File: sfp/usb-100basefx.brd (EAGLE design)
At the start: 54 x 29 mm, 52 parts, among them IC1 LD33, IC2 93LC66SN, U1 AX88772BSP, U2 SFP, Y1 25MHz

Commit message: there's a cat on my pcb...
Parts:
- added U$2, U$4, U$8: (no value), cat:CAT-L
- added U$3, U$5, U$7: (no value), cat:CAT-R
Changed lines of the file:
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@@
 <element name="R1" library="rcl" package="R0603" value="0" x="15.6464" y="8.9408" rot="MR0"/>
 <element name="R3" library="rcl" package="R0603" value="0" x="15.6464" y="7.5184" rot="MR0"/>
+<element name="U$2" library="cat" package="CAT-L" value="" x="12.192" y="27.0256" rot="R270"/>
+<element name="U$3" library="cat" package="CAT-R" value="" x="19.1008" y="23.9776" rot="R270"/>
+<element name="U$4" library="cat" package="CAT-L" value="" x="23.5712" y="27.0256" rot="R270"/>
+<element name="U$5" library="cat" package="CAT-R" value="" x="27.6352" y="24.9936" rot="R270"/>
+<element name="U$7" library="cat" package="CAT-R" value="" x="42.2656" y="24.5872" rot="R270"/>
+<element name="U$8" library="cat" package="CAT-L" value="" x="45.5168" y="27.0256" rot="R270"/>
 </elements>
 <signals>

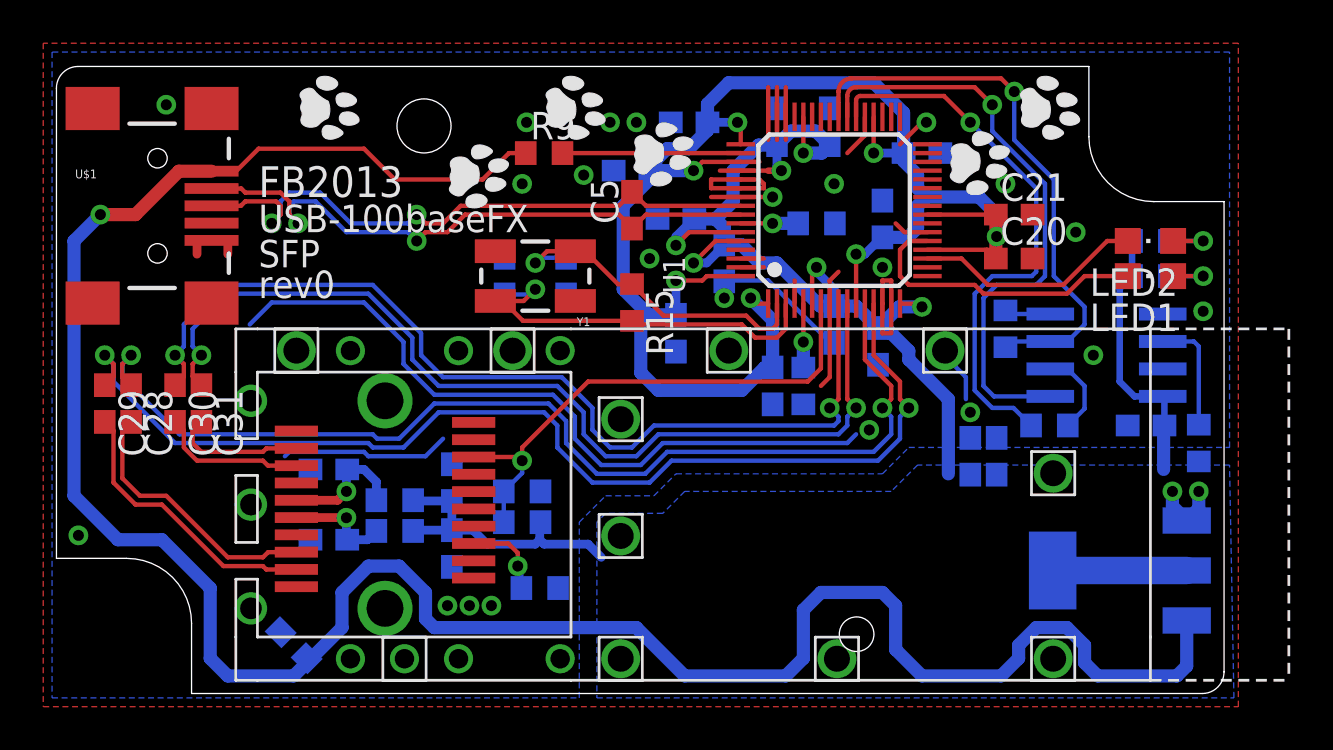
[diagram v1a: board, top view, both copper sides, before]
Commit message: rev1: fix sd signal logic level
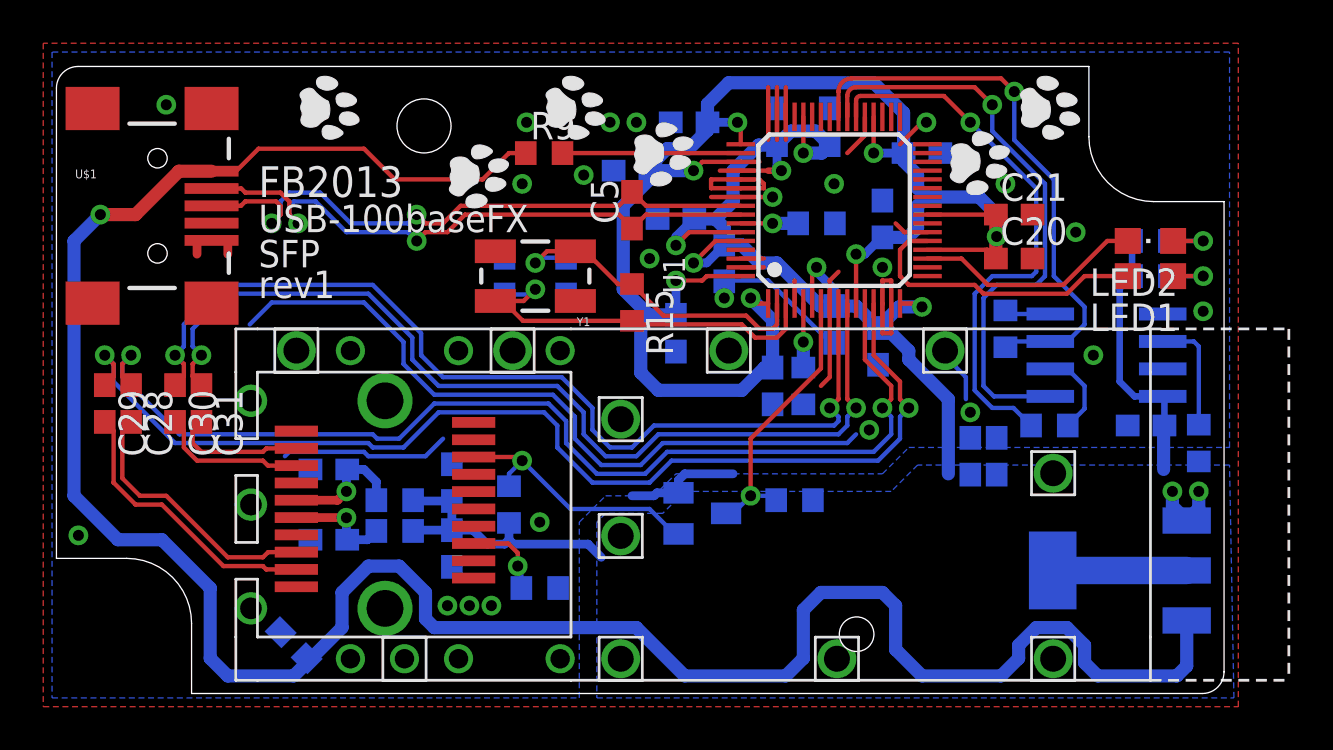
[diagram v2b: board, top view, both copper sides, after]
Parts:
- added Q1: MOSFET-NCHANNELBSS123LT1G, SparkFun-DiscreteSemi:SOT23
- moved R21 12.6 mm to (34.1, 8.94), turned to 0 degrees
- moved R20 1.02 mm to (20.9, 8.74), turned to 90 degrees
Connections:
- new net SD_OUT: Q1.3, R21.2, U1.7
- net GND: now also Q1.2; no longer R21.2
- net SD: now also Q1.1; no longer R21.1, U1.7
- net VCC: now also R21.1
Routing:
- net SD_OUT: track 0.00 -> 13.0 mm, vias 0 -> 1
- net SD: track 24.4 -> 12.4 mm
- net GND: track 90.2 -> 95.7 mm, vias 24 -> 25
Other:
- board text added: "rev1"
- board text removed: "rev0"
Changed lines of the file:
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@@
 <text x="9.3472" y="21.336" size="1.27" layer="121">USB-100baseFX</text>
 <text x="9.3472" y="19.7104" size="1.27" layer="121">SFP</text>
-<text x="9.3472" y="18.288" size="1.27" layer="121">rev0</text>
+<text x="9.3472" y="18.288" size="1.27" layer="121">rev1</text>
 <hole x="37.0078" y="2.7432" drill="1.6"/>
 </plain>
@@
 <element name="C26" library="rcl" package="C0603" value=".1u" x="40.0304" y="24.9936" rot="MR180"/>
 <element name="C27" library="rcl" package="C0603" value=".1u" x="42.2656" y="10.9728" rot="MR90"/>
-<element name="R20" library="rcl" package="R0603" value="130" x="21.5392" y="7.9248" rot="MR0"/>
-<element name="R21" library="rcl" package="R0603" value="82" x="21.5392" y="9.3472" rot="MR180"/>
+<element name="R20" library="rcl" package="R0603" value="130" x="20.9296" y="8.7376" rot="MR90"/>
+<element name="R21" library="rcl" package="R0603" value="82" x="34.1376" y="8.9408" rot="MR0"/>
 <element name="IC1" library="SparkFun-PowerIC" package="SOT223" value="LD33" x="49.1744" y="5.6896" rot="MR270"/>
 <element name="C9" library="rcl" package="C0603" value=".1u" x="18.288" y="6.7056" rot="MR270"/>
@@
 <element name="U$7" library="cat" package="CAT-R" value="" x="42.2656" y="24.5872" rot="R270"/>
 <element name="U$8" library="cat" package="CAT-L" value="" x="45.5168" y="27.0256" rot="R270"/>
+<element name="Q1" library="SparkFun-DiscreteSemi" package="SOT23" value="MOSFET-NCHANNELBSS123LT1G" x="29.8704" y="8.3312" rot="MR90">
+<attribute name="PROD_ID" value="TRANS-08345" x="29.8704" y="8.3312" size="1.778" layer="28" rot="MR90" display="off"/>
+</element>
 </elements>
 <signals>
@@
 <wire x1="18.288" y1="7.5556" x2="19.2668" y2="7.5556" width="0.4064" layer="16"/>
 <wire x1="19.2668" y1="7.5556" x2="19.9136" y2="6.9088" width="0.4064" layer="16"/>
-<wire x1="19.9136" y1="6.9088" x2="22.1488" y2="6.9088" width="0.4064" layer="16"/>
-<wire x1="22.1488" y1="6.9088" x2="22.352" y2="7.112" width="0.4064" layer="16"/>
-<wire x1="22.352" y1="7.112" x2="22.5552" y2="6.9088" width="0.4064" layer="16"/>
-<wire x1="22.5552" y1="6.9088" x2="24.5872" y2="6.9088" width="0.4064" layer="16"/>
+<wire x1="19.9136" y1="6.9088" x2="20.7264" y2="6.9088" width="0.4064" layer="16"/>
+<wire x1="20.7264" y1="6.9088" x2="20.9296" y2="7.112" width="0.4064" layer="16"/>
+<wire x1="20.9296" y1="7.112" x2="21.1328" y2="6.9088" width="0.4064" layer="16"/>
+<wire x1="21.1328" y1="6.9088" x2="24.5872" y2="6.9088" width="0.4064" layer="16"/>
 <wire x1="24.5872" y1="6.9088" x2="25.1968" y2="6.2992" width="0.4064" layer="16"/>
-<wire x1="22.352" y1="7.112" x2="22.352" y2="7.8876" width="0.4064" layer="16"/>
-<wire x1="22.352" y1="7.8876" x2="22.3892" y2="7.9248" width="0.4064" layer="16"/>
 <wire x1="39.4208" y1="15.8496" x2="39.4208" y2="15.4432" width="0.6096" layer="16"/>
 <wire x1="39.4208" y1="15.4432" x2="41.2496" y2="13.6144" width="0.6096" layer="16"/>
@@
 <wire x1="18.288" y1="8.9036" x2="16.5336" y2="8.9036" width="0.4064" layer="16"/>
 <wire x1="16.5336" y1="8.9036" x2="16.4964" y2="8.9408" width="0.4064" layer="16"/>
+<contactref element="R21" pad="1"/>
+<wire x1="20.9296" y1="7.112" x2="20.9296" y2="7.8876" width="0.4064" layer="16"/>
 </signal>
 <signal name="GND">
@@
 <contactref element="C27" pad="2"/>
 <via x="5.08" y="27.2288" extent="1-16" drill="0.508"/>
-<contactref element="R21" pad="2"/>
 <contactref element="IC1" pad="1"/>
 <wire x1="7.9248" y1="20.9552" x2="7.9248" y2="20.32" width="0.4064" layer="1"/>
@@
 <wire x1="35.7632" y1="18.034" x2="35.7632" y2="14.6304" width="0.2032" layer="1"/>
 <wire x1="35.7632" y1="14.6304" x2="35.3568" y2="14.224" width="0.2032" layer="1"/>
+<contactref element="Q1" pad="2"/>
+<via x="22.352" y="7.9248" extent="1-16" drill="0.508"/>
+<wire x1="28.7704" y1="9.2812" x2="27.7724" y2="9.2812" width="0.4064" layer="16"/>
+<wire x1="28.7704" y1="9.2812" x2="28.7704" y2="9.8728" width="0.4064" layer="16"/>
+<wire x1="28.7704" y1="9.8728" x2="29.0576" y2="10.16" width="0.4064" layer="16"/>
+<wire x1="29.0576" y1="10.16" x2="31.2928" y2="10.16" width="0.4064" layer="16"/>
+<wire x1="27.7724" y1="9.2812" x2="27.6352" y2="9.144" width="0.4064" layer="16"/>
+<wire x1="27.6352" y1="9.144" x2="26.6192" y2="9.144" width="0.4064" layer="16"/>
 </signal>
 <signal name="TD_DP">
@@
 </signal>
 <signal name="SD">
-<contactref element="U1" pad="7"/>
-<contactref element="R21" pad="1"/>
 <contactref element="R20" pad="2"/>
-<wire x1="20.6892" y1="9.3472" x2="20.6892" y2="7.9248" width="0.2032" layer="16"/>
-<wire x1="35.3568" y1="18.034" x2="35.3568" y2="15.0368" width="0.2032" layer="1"/>
 <contactref element="U2" pad="8"/>
 <via x="21.5392" y="10.7696" extent="1-16" drill="0.508"/>
-<wire x1="35.3568" y1="15.0368" x2="34.7472" y2="14.4272" width="0.2032" layer="1"/>
-<wire x1="34.7472" y1="14.4272" x2="24.5872" y2="14.4272" width="0.2032" layer="1"/>
-<wire x1="24.5872" y1="14.4272" x2="21.5392" y2="11.3792" width="0.2032" layer="1"/>
-<wire x1="21.5392" y1="11.3792" x2="21.5392" y2="10.7696" width="0.2032" layer="1"/>
-<wire x1="20.6892" y1="9.3472" x2="21.5392" y2="10.1972" width="0.2032" layer="16"/>
-<wire x1="21.5392" y1="10.1972" x2="21.5392" y2="10.7696" width="0.2032" layer="16"/>
 <wire x1="19.2968" y1="10.9376" x2="21.3712" y2="10.9376" width="0.2032" layer="1"/>
 <wire x1="21.3712" y1="10.9376" x2="21.5392" y2="10.7696" width="0.2032" layer="1"/>
+<contactref element="Q1" pad="1"/>
+<wire x1="20.9296" y1="9.5876" x2="20.9296" y2="10.16" width="0.2032" layer="16"/>
+<wire x1="20.9296" y1="10.16" x2="21.5392" y2="10.7696" width="0.2032" layer="16"/>
+<wire x1="21.5392" y1="10.7696" x2="23.7744" y2="8.5344" width="0.2032" layer="16"/>
+<wire x1="23.7744" y1="8.5344" x2="27.432" y2="8.5344" width="0.2032" layer="16"/>
+<wire x1="27.432" y1="8.5344" x2="28.2448" y2="7.7216" width="0.2032" layer="16"/>
+<wire x1="28.2448" y1="7.7216" x2="28.43" y2="7.7216" width="0.2032" layer="16"/>
+<wire x1="28.43" y1="7.7216" x2="28.7704" y2="7.3812" width="0.2032" layer="16"/>
 </signal>
 <signal name="USB_DM">
@@
 <wire x1="14.39" y1="7.112" x2="14.7964" y2="7.5184" width="0.4064" layer="16"/>
 </signal>
+<signal name="SD_OUT">
+<contactref element="Q1" pad="3"/>
+<contactref element="R21" pad="2"/>
+<contactref element="U1" pad="7"/>
+<wire x1="35.3568" y1="18.034" x2="35.3568" y2="15.0368" width="0.2032" layer="1"/>
+<wire x1="30.9704" y1="8.3312" x2="31.2928" y2="8.3312" width="0.2032" layer="16"/>
+<wire x1="31.2928" y1="8.3312" x2="32.1056" y2="9.144" width="0.2032" layer="16"/>
+<wire x1="33.2876" y1="8.9408" x2="33.0844" y2="9.144" width="0.2032" layer="16"/>
+<wire x1="33.0844" y1="9.144" x2="32.1056" y2="9.144" width="0.2032" layer="16"/>
+<via x="32.1056" y="9.144" extent="1-16" drill="0.508"/>
+<wire x1="35.3568" y1="15.0368" x2="32.1056" y2="11.7856" width="0.2032" layer="1"/>
+<wire x1="32.1056" y1="11.7856" x2="32.1056" y2="9.144" width="0.2032" layer="1"/>
+</signal>
 </signals>

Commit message: sfp: schematic cleanup
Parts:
- Q1: value MOSFET-NCHANNELBSS123LT1G -> BSS138
- R20: value 130 -> 4k7
- R21: value 82 -> 4k7
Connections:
- net SD_OUT renamed SD_N
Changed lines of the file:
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@@
 <element name="C26" library="rcl" package="C0603" value=".1u" x="40.0304" y="24.9936" rot="MR180"/>
 <element name="C27" library="rcl" package="C0603" value=".1u" x="42.2656" y="10.9728" rot="MR90"/>
-<element name="R20" library="rcl" package="R0603" value="130" x="20.9296" y="8.7376" rot="MR90"/>
-<element name="R21" library="rcl" package="R0603" value="82" x="34.1376" y="8.9408" rot="MR0"/>
+<element name="R20" library="rcl" package="R0603" value="4k7" x="20.9296" y="8.7376" rot="MR90"/>
+<element name="R21" library="rcl" package="R0603" value="4k7" x="34.1376" y="8.9408" rot="MR0"/>
 <element name="IC1" library="SparkFun-PowerIC" package="SOT223" value="LD33" x="49.1744" y="5.6896" rot="MR270"/>
 <element name="C9" library="rcl" package="C0603" value=".1u" x="18.288" y="6.7056" rot="MR270"/>
@@
 <element name="U$7" library="cat" package="CAT-R" value="" x="42.2656" y="24.5872" rot="R270"/>
 <element name="U$8" library="cat" package="CAT-L" value="" x="45.5168" y="27.0256" rot="R270"/>
-<element name="Q1" library="SparkFun-DiscreteSemi" package="SOT23" value="MOSFET-NCHANNELBSS123LT1G" x="29.8704" y="8.3312" rot="MR90">
+<element name="Q1" library="SparkFun-DiscreteSemi" package="SOT23" value="BSS138" x="29.8704" y="8.3312" rot="MR90">
 <attribute name="PROD_ID" value="TRANS-08345" x="29.8704" y="8.3312" size="1.778" layer="28" rot="MR90" display="off"/>
 </element>
@@
 <wire x1="14.39" y1="7.112" x2="14.7964" y2="7.5184" width="0.4064" layer="16"/>
 </signal>
-<signal name="SD_OUT">
+<signal name="SD_N">
 <contactref element="Q1" pad="3"/>
 <contactref element="R21" pad="2"/>

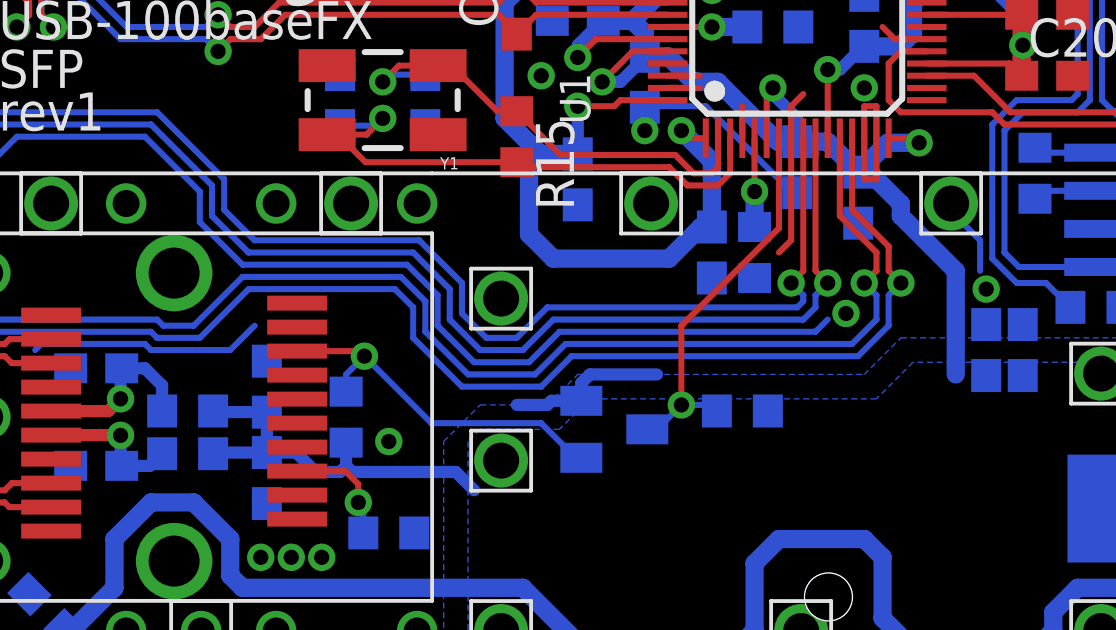
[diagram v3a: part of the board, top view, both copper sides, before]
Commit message: add some vias and close a ground plane
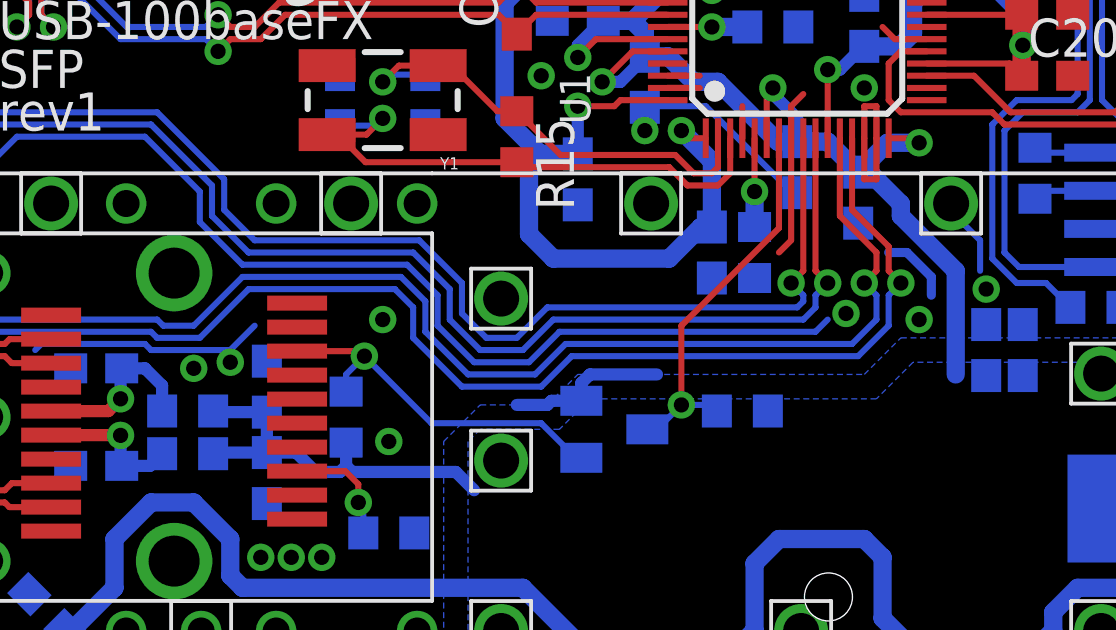
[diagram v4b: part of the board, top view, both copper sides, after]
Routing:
- net GND: track 95.7 -> 98.0 mm, vias 25 -> 29
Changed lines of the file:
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@@
 <wire x1="27.7724" y1="9.2812" x2="27.6352" y2="9.144" width="0.4064" layer="16"/>
 <wire x1="27.6352" y1="9.144" x2="26.6192" y2="9.144" width="0.4064" layer="16"/>
+<via x="17.0688" y="10.5664" extent="1-16" drill="0.508"/>
+<via x="15.8496" y="10.3632" extent="1-16" drill="0.508"/>
+<via x="22.1488" y="11.9888" extent="1-16" drill="0.508"/>
+<wire x1="40.4368" y1="13.4112" x2="39.624" y2="14.224" width="0.3048" layer="16"/>
+<wire x1="39.624" y1="14.224" x2="39.0144" y2="14.224" width="0.3048" layer="16"/>
+<wire x1="40.4368" y1="13.4112" x2="40.4368" y2="12.8016" width="0.3048" layer="16"/>
+<via x="40.0304" y="11.9888" extent="1-16" drill="0.508"/>
 </signal>
 <signal name="TD_DP">

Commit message: sfp: change cap to 33p
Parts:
- C7, C8: value 18p -> 33p
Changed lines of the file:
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@@
 <element name="R14" library="rcl" package="R0603" value="22" x="43.8912" y="16.8656" rot="MR270"/>
 <element name="Y1" library="SparkFun-FreqCtrl" package="CRYSTAL-SMD-5X3" value="25MHz" x="22.1488" y="19.304" rot="R180"/>
-<element name="C7" library="rcl" package="C0603" value="18p" x="23.5712" y="19.304" rot="MR270"/>
-<element name="C8" library="rcl" package="C0603" value="18p" x="20.7264" y="19.304" rot="MR90"/>
+<element name="C7" library="rcl" package="C0603" value="33p" x="23.5712" y="19.304" rot="MR270"/>
+<element name="C8" library="rcl" package="C0603" value="33p" x="20.7264" y="19.304" rot="MR90"/>
 <element name="R15" library="rcl" package="R0603" value="1M" x="26.6192" y="18.0848" rot="R270"/>
 <element name="LED2" library="led" package="CHIPLED_0805" value="" x="50.5968" y="20.9296" rot="R90"/>
